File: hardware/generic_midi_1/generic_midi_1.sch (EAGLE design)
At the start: 26 parts, among them IC1 MEGA168/328, IC2 RFM12

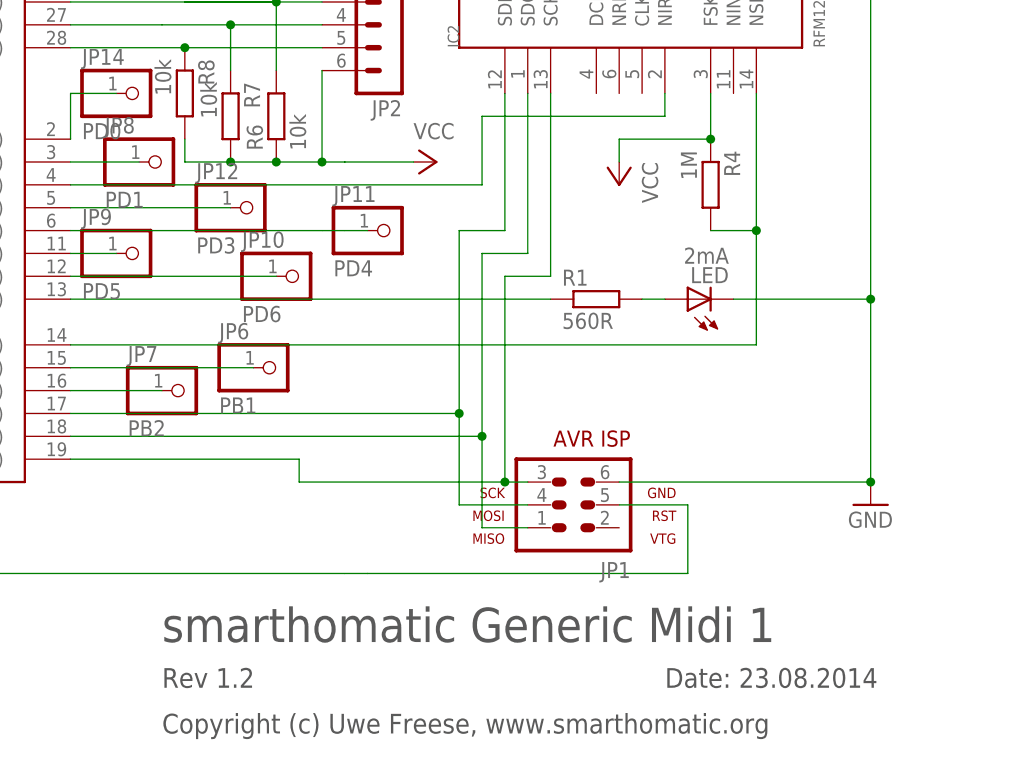
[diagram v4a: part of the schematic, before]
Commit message: Add pull-up resistor for possible one-wire sensor on PD4.
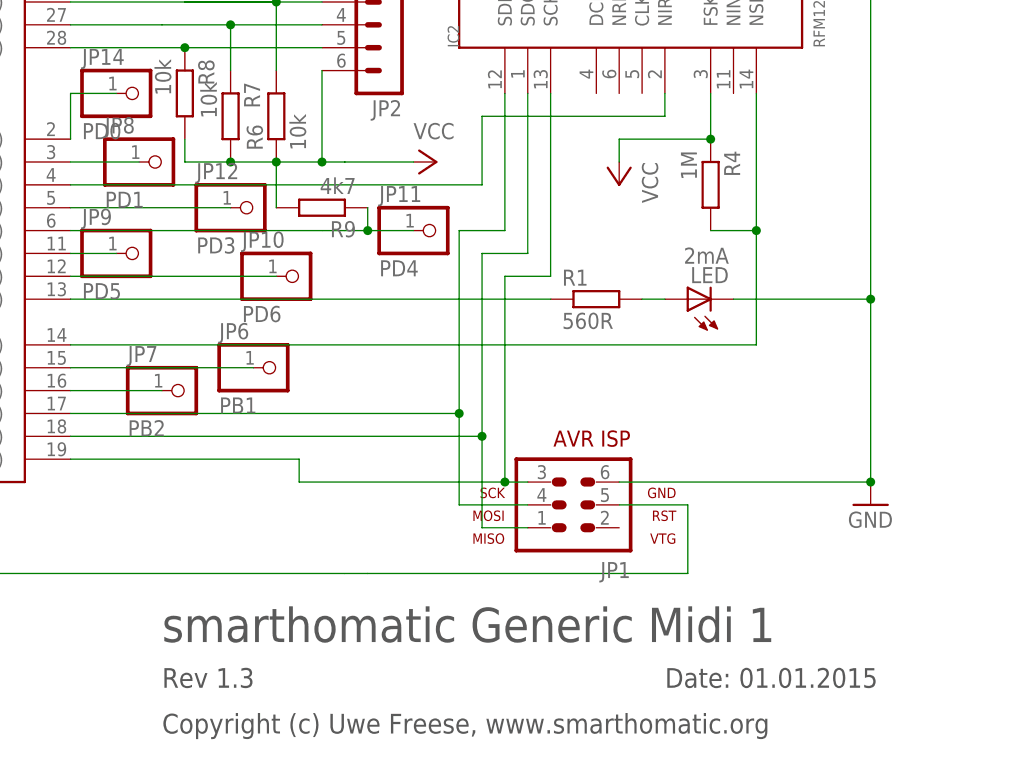
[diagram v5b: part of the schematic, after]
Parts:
- added R9: 4k7, rcl:R-EU_0207/7
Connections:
- net N$22: now also R9.1
- net VCC: now also R9.2
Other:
- note added: "Date: 01.01.2015"
- note added: "Rev 1.3"
- note removed: "Date: 23.08.2014"
- note removed: "Rev 1.2"
- moved on the sheet: JP11
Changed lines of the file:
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@@
 <part name="JP13" library="pinhead" deviceset="PINHD-1X1" device="" value="PB7"/>
 <part name="JP14" library="pinhead" deviceset="PINHD-1X1" device="" value="PD0"/>
+<part name="R9" library="rcl" deviceset="R-EU_" device="0207/7" value="4k7"/>
 </parts>
 <sheets>
@@
 <frame x1="-60.96" y1="-53.34" x2="132.08" y2="88.9" columns="8" rows="5" layer="97"/>
 <text x="40.64" y="-33.02" size="3.81" layer="97">smarthomatic Generic Midi 1</text>
-<text x="96.52" y="-38.1" size="2.1844" layer="97">Date: 23.08.2014</text>
-<text x="40.64" y="-38.1" size="2.1844" layer="97">Rev 1.2</text>
+<text x="96.52" y="-38.1" size="2.1844" layer="97">Date: 01.01.2015</text>
+<text x="40.64" y="-38.1" size="2.1844" layer="97">Rev 1.3</text>
 <text x="40.64" y="-43.18" size="2.1844" layer="97">Copyright (c) Uwe Freese, www.smarthomatic.org</text>
 </plain>
@@
 <instance part="R7" gate="G$1" x="48.26" y="25.4" rot="R270"/>
 <instance part="R8" gate="G$1" x="43.18" y="27.94" rot="R270"/>
-<instance part="JP11" gate="G$1" x="66.04" y="12.7"/>
+<instance part="JP11" gate="G$1" x="71.12" y="12.7"/>
 <instance part="JP12" gate="G$1" x="50.8" y="15.24"/>
 <instance part="JP13" gate="G$1" x="-43.18" y="25.4" rot="R180"/>
 <instance part="JP14" gate="G$1" x="38.1" y="27.94"/>
+<instance part="R9" gate="G$1" x="58.42" y="15.24" rot="R180"/>
 </instances>
 <busses>
@@
 <junction x="53.34" y="20.32"/>
 <pinref part="JP2" gate="1" pin="6"/>
+<pinref part="R9" gate="G$1" pin="2"/>
+<wire x1="53.34" y1="15.24" x2="53.34" y2="20.32" width="0.1524" layer="91"/>
 </segment>
 </net>
@@
 <wire x1="58.42" y1="12.7" x2="60.96" y2="12.7" width="0.1524" layer="91"/>
 <wire x1="60.96" y1="12.7" x2="63.5" y2="12.7" width="0.1524" layer="91"/>
-</segment>
-</net>
+<pinref part="R9" gate="G$1" pin="1"/>
+<wire x1="63.5" y1="12.7" x2="68.58" y2="12.7" width="0.1524" layer="91"/>
+<wire x1="63.5" y1="15.24" x2="63.5" y2="12.7" width="0.1524" layer="91"/>
+<junction x="63.5" y="12.7"/>
+</segment>
+</net>

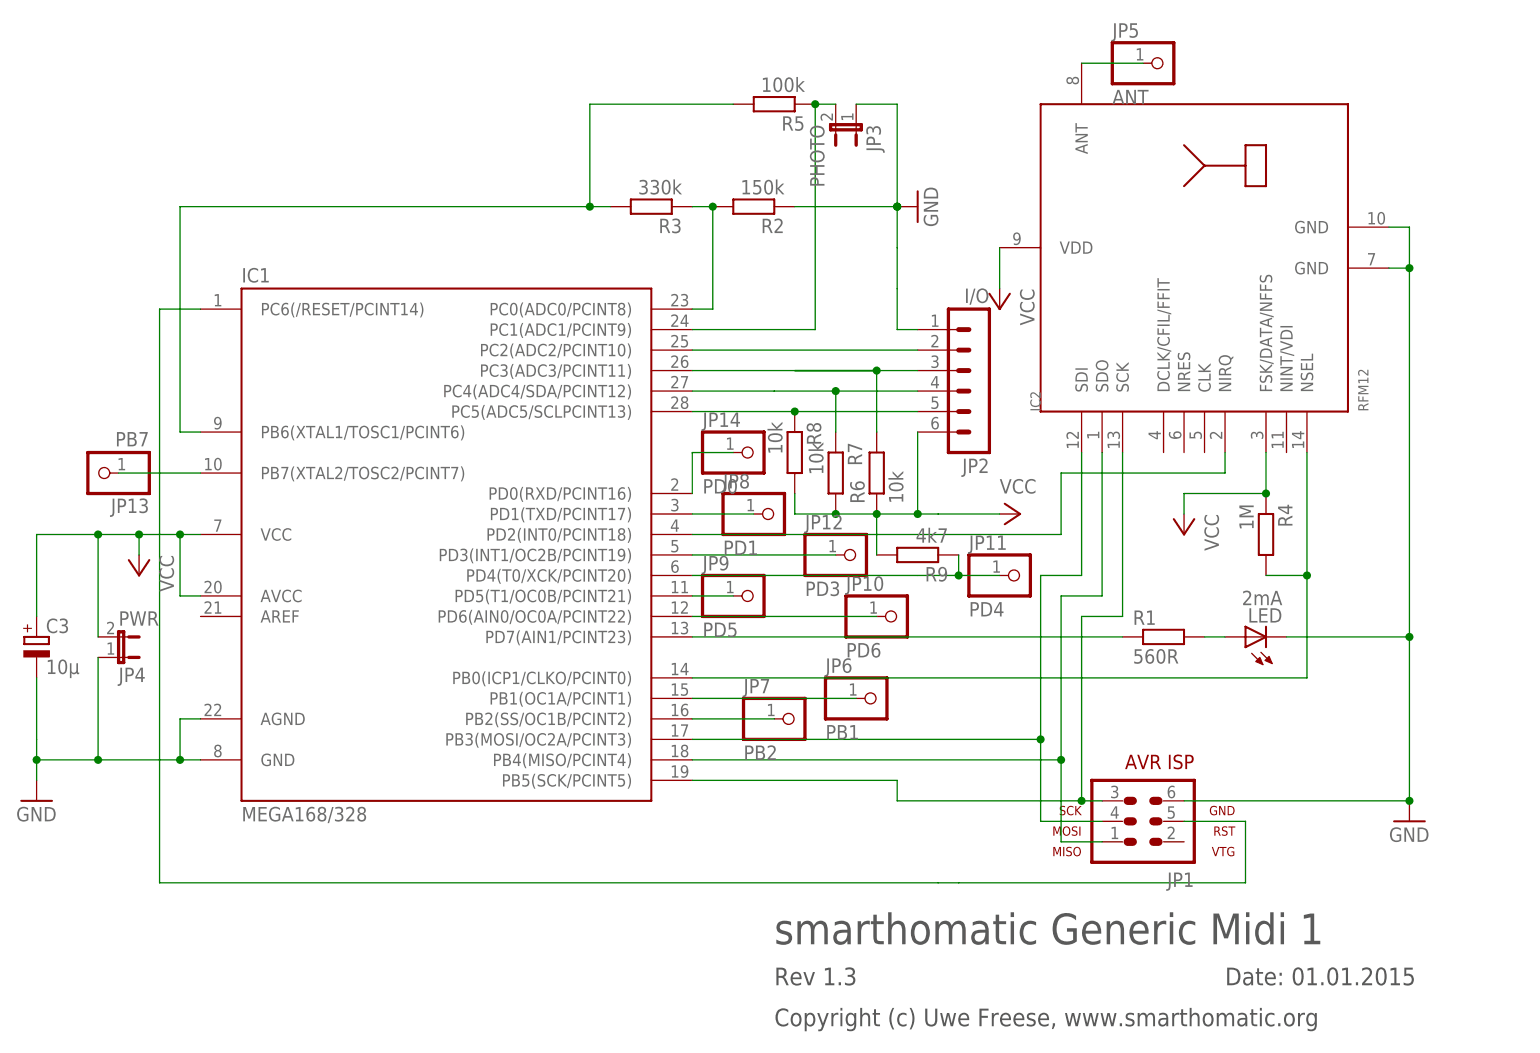
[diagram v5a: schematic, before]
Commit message: Add solder jumper to PCB for ISP VCC pin.
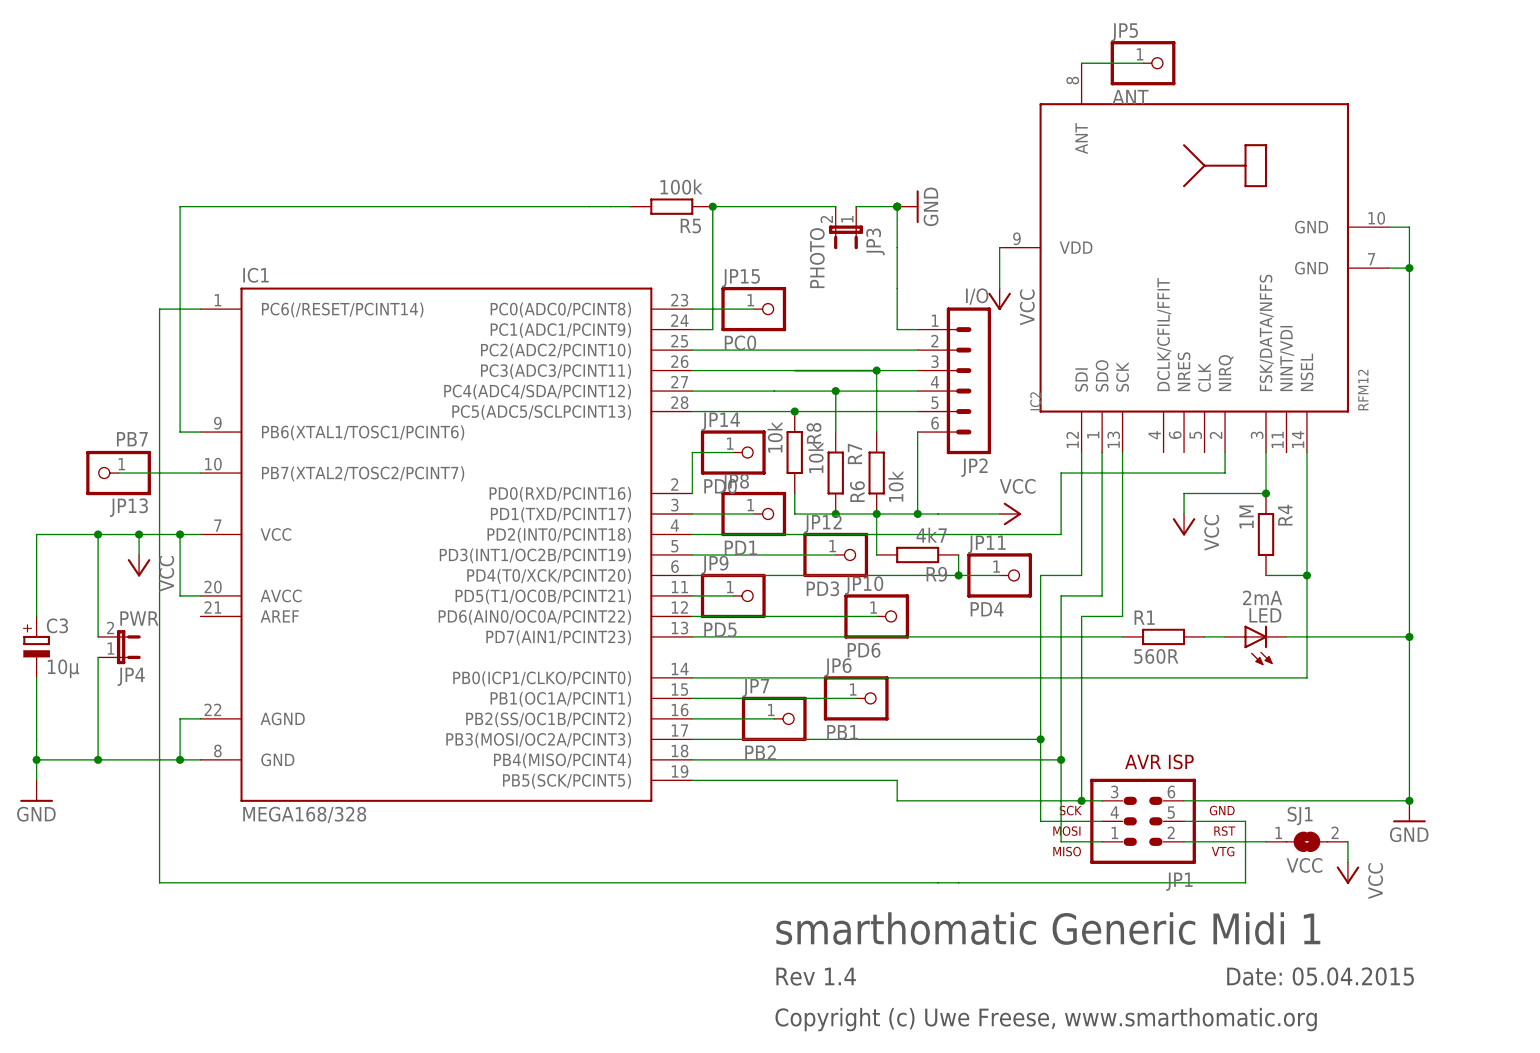
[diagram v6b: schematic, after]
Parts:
- removed R2: 150k, rcl:R-EU_0207/7
- removed R3: 330k, rcl:R-EU_0207/7
- added JP15: PC0, pinhead:PINHD-1X1
- added SJ1: VCC, jumper:SJ
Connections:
- new net N$27: JP1.2, SJ1.1
- net GND: no longer R2.1
- net N$18: now also JP15.1; no longer R2.2, R3.1
- net N$24: no longer R3.2
- net VCC: now also SJ1.2
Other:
- note added: "Date: 05.04.2015"
- note added: "Rev 1.4"
- note removed: "Date: 01.01.2015"
- note removed: "Rev 1.3"
- moved on the sheet: JP3, R5
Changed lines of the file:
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@@
 <part name="C3" library="rcl" deviceset="CPOL-EU" device="E1.8-4" value="10µ"/>
 <part name="P+3" library="supply1" deviceset="VCC" device=""/>
-<part name="R2" library="rcl" deviceset="R-EU_" device="0207/7" value="150k"/>
-<part name="R3" library="rcl" deviceset="R-EU_" device="0207/7" value="330k"/>
 <part name="GND3" library="supply1" deviceset="GND" device=""/>
 <part name="R4" library="rcl" deviceset="R-EU_" device="0207/7" value="1M"/>
@@
 <part name="JP14" library="pinhead" deviceset="PINHD-1X1" device="" value="PD0"/>
 <part name="R9" library="rcl" deviceset="R-EU_" device="0207/7" value="4k7"/>
+<part name="SJ1" library="jumper" deviceset="SJ" device="" value="VCC"/>
+<part name="P+5" library="supply1" deviceset="VCC" device=""/>
+<part name="JP15" library="pinhead" deviceset="PINHD-1X1" device="" value="PC0"/>
 </parts>
 <sheets>
@@
 <frame x1="-60.96" y1="-53.34" x2="132.08" y2="88.9" columns="8" rows="5" layer="97"/>
 <text x="40.64" y="-33.02" size="3.81" layer="97">smarthomatic Generic Midi 1</text>
-<text x="96.52" y="-38.1" size="2.1844" layer="97">Date: 01.01.2015</text>
-<text x="40.64" y="-38.1" size="2.1844" layer="97">Rev 1.3</text>
+<text x="96.52" y="-38.1" size="2.1844" layer="97">Date: 05.04.2015</text>
+<text x="40.64" y="-38.1" size="2.1844" layer="97">Rev 1.4</text>
 <text x="40.64" y="-43.18" size="2.1844" layer="97">Copyright (c) Uwe Freese, www.smarthomatic.org</text>
 </plain>
@@
 <instance part="C3" gate="G$1" x="-50.8" y="5.08"/>
 <instance part="P+3" gate="VCC" x="68.58" y="45.72" rot="R180"/>
-<instance part="R2" gate="G$1" x="38.1" y="58.42" rot="R180"/>
-<instance part="R3" gate="G$1" x="25.4" y="58.42" rot="R180"/>
 <instance part="GND3" gate="1" x="58.42" y="58.42" rot="R90"/>
 <instance part="R4" gate="G$1" x="101.6" y="17.78" rot="R270"/>
 <instance part="JP2" gate="1" x="66.04" y="35.56" rot="R180"/>
-<instance part="R5" gate="G$1" x="40.64" y="71.12" rot="R180"/>
-<instance part="JP3" gate="A" x="50.8" y="68.58" rot="R180"/>
+<instance part="R5" gate="G$1" x="27.94" y="58.42" rot="R180"/>
+<instance part="JP3" gate="A" x="50.8" y="55.88" rot="R180"/>
 <instance part="P+4" gate="VCC" x="71.12" y="20.32" rot="R270"/>
 <instance part="JP4" gate="A" x="-40.64" y="2.54" rot="MR90"/>
@@
 <instance part="JP14" gate="G$1" x="38.1" y="27.94"/>
 <instance part="R9" gate="G$1" x="58.42" y="15.24" rot="R180"/>
+<instance part="SJ1" gate="1" x="106.68" y="-20.32"/>
+<instance part="P+5" gate="VCC" x="111.76" y="-25.4" rot="R180"/>
+<instance part="JP15" gate="G$1" x="40.64" y="45.72"/>
 </instances>
 <busses>
@@
 </segment>
 <segment>
-<pinref part="R2" gate="G$1" pin="1"/>
 <pinref part="GND3" gate="1" pin="GND"/>
-<wire x1="43.18" y1="58.42" x2="55.88" y2="58.42" width="0.1524" layer="91"/>
 <pinref part="JP3" gate="A" pin="1"/>
-<wire x1="50.8" y1="71.12" x2="55.88" y2="71.12" width="0.1524" layer="91"/>
-<wire x1="55.88" y1="71.12" x2="55.88" y2="58.42" width="0.1524" layer="91"/>
+<wire x1="50.8" y1="58.42" x2="55.88" y2="58.42" width="0.1524" layer="91"/>
 <junction x="55.88" y="58.42"/>
 <pinref part="JP2" gate="1" pin="1"/>
@@
 <wire x1="53.34" y1="15.24" x2="53.34" y2="20.32" width="0.1524" layer="91"/>
 </segment>
+<segment>
+<pinref part="SJ1" gate="1" pin="2"/>
+<pinref part="P+5" gate="VCC" pin="VCC"/>
+<wire x1="111.76" y1="-20.32" x2="111.76" y2="-22.86" width="0.1524" layer="91"/>
+</segment>
 </net>
 <net name="N$3" class="0">
@@
 </segment>
 </net>
-<net name="N$18" class="0">
-<segment>
-<pinref part="R3" gate="G$1" pin="1"/>
-<pinref part="R2" gate="G$1" pin="2"/>
-<wire x1="30.48" y1="58.42" x2="33.02" y2="58.42" width="0.1524" layer="91"/>
-<pinref part="IC1" gate="1" pin="PC0(ADC0/PCINT8)"/>
-<wire x1="30.48" y1="45.72" x2="33.02" y2="45.72" width="0.1524" layer="91"/>
-<wire x1="33.02" y1="45.72" x2="33.02" y2="58.42" width="0.1524" layer="91"/>
-<junction x="33.02" y="58.42"/>
-</segment>
-</net>
 <net name="N$1" class="0">
 <segment>
 <pinref part="R5" gate="G$1" pin="1"/>
 <pinref part="JP3" gate="A" pin="2"/>
-<wire x1="45.72" y1="71.12" x2="48.26" y2="71.12" width="0.1524" layer="91"/>
-<wire x1="45.72" y1="71.12" x2="45.72" y2="43.18" width="0.1524" layer="91"/>
-<junction x="45.72" y="71.12"/>
+<wire x1="33.02" y1="58.42" x2="48.26" y2="58.42" width="0.1524" layer="91"/>
+<wire x1="33.02" y1="58.42" x2="33.02" y2="43.18" width="0.1524" layer="91"/>
+<junction x="33.02" y="58.42"/>
 <pinref part="IC1" gate="1" pin="PC1(ADC1/PCINT9)"/>
-<wire x1="45.72" y1="43.18" x2="30.48" y2="43.18" width="0.1524" layer="91"/>
+<wire x1="33.02" y1="43.18" x2="30.48" y2="43.18" width="0.1524" layer="91"/>
 </segment>
 </net>
@@
 <net name="N$24" class="0">
 <segment>
-<pinref part="R3" gate="G$1" pin="2"/>
-<wire x1="20.32" y1="58.42" x2="17.78" y2="58.42" width="0.1524" layer="91"/>
-<wire x1="17.78" y1="58.42" x2="17.78" y2="71.12" width="0.1524" layer="91"/>
+<wire x1="17.78" y1="58.42" x2="20.32" y2="58.42" width="0.1524" layer="91"/>
 <pinref part="R5" gate="G$1" pin="2"/>
-<wire x1="17.78" y1="71.12" x2="35.56" y2="71.12" width="0.1524" layer="91"/>
+<wire x1="20.32" y1="58.42" x2="22.86" y2="58.42" width="0.1524" layer="91"/>
 <pinref part="IC1" gate="1" pin="PB6(XTAL1/TOSC1/PCINT6)"/>
 <wire x1="-30.48" y1="30.48" x2="-33.02" y2="30.48" width="0.1524" layer="91"/>
 <wire x1="-33.02" y1="30.48" x2="-33.02" y2="58.42" width="0.1524" layer="91"/>
 <wire x1="17.78" y1="58.42" x2="-33.02" y2="58.42" width="0.1524" layer="91"/>
-<junction x="17.78" y="58.42"/>
 </segment>
 </net>
@@
 </segment>
 </net>
+<net name="N$27" class="0">
+<segment>
+<pinref part="JP1" gate="G$1" pin="2"/>
+<pinref part="SJ1" gate="1" pin="1"/>
+<wire x1="91.44" y1="-20.32" x2="101.6" y2="-20.32" width="0.1524" layer="91"/>
+</segment>
+</net>
+<net name="N$18" class="0">
+<segment>
+<pinref part="IC1" gate="1" pin="PC0(ADC0/PCINT8)"/>
+<pinref part="JP15" gate="G$1" pin="1"/>
+<wire x1="30.48" y1="45.72" x2="38.1" y2="45.72" width="0.1524" layer="91"/>
+</segment>
+</net>
